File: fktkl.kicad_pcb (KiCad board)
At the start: 2 copper layers, 342.6 x 94.5 mm, 160 parts, among them K1 SCaps, K10 Z, K11 Super, K12 2, K13 W, K14 S, K15 X, K16 Alt, K17 3, K18 E, K19 D, K2 Esc, K20 C, K21 Space, K22 4, K23 R, K24 F, K25 V, K26 AltGr, K26 Space, K27 5, K28 T, K29 G, K3 Tab, K30 B, K31 Ctrl, K32 6, K33 Y, K34 H, K35 N, K36 Super, K37 7, K38 U, K39 J, K4 Caps, K40 M, K41 Left, K42 8, K43 I, K44 K, K45 ,, K46 Down, K47 9, K48 O, K49 L, K5 Shift, K50 ., K51 Right, K52 0, K53 P, K54 :, K55 -, K56 [, K57 ", K58 =, K59 ], K6 Ctrl, K60 /, K61 Yen, K62 |, K63 Shift, K64 BS, K65 Del, K66 Fn, K67 Ins, K68 Enter, K69 C3, K7 1, K70 Home, K71 C0, K72 Up, K73 PgUp, K74 C1, K75 C4, K76 End, K77 C2, K78 PgDwn, K8 Q, K9 A, U1 ProMicro

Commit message: connected row7
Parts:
- K26: value Space -> AltGr
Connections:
- U1 pad 14: Net-(U1-Pad14) -> /row7
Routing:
- net /row7: track 143.2 -> 237.0 mm
- net GND: track 95.5 -> 130.8 mm, vias 14 -> 16
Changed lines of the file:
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@@
 (kicad_pcb (version 4) (host pcbnew 4.0.7)
   (general
-    (links 548)
+    (links 549)
     (no_connects 0)
     (area 30.805779 28.7814 378.767951 126.494201)
     (thickness 1.6)
     (drawings 10)
-    (tracks 718)
+    (tracks 734)
     (zones 0)
     (modules 160)
-    (nets 101)
+    (nets 100)
   )
   (page A3)
@@
     (pad_to_mask_clearance 0.2)
     (aux_axis_origin 0 0)
-    (visible_elements 7FFFF77F)
+    (visible_elements 7FFFFFFF)
     (pcbplotparams
       (layerselection 0x010fc_80000001)
@@
   (net 96 /row7)
   (net 97 "Net-(U1-Pad1)")
-  (net 98 "Net-(U1-Pad14)")
-  (net 99 VCC)
-  (net 100 "Net-(Reset1-Pad2)")
+  (net 98 VCC)
+  (net 99 "Net-(Reset1-Pad2)")
   (net_class Default "This is the default net class."
     (clearance 0.2)
@@
     (add_net "Net-(Reset1-Pad2)")
     (add_net "Net-(U1-Pad1)")
-    (add_net "Net-(U1-Pad14)")
     (add_net VCC)
   )
@@
       (effects (font (size 1 1) (thickness 0.2)))
     )
-    (fp_text value Space (at 0 4.572) (layer F.SilkS)
+    (fp_text value AltGr (at 0 4.572) (layer F.SilkS)
       (effects (font (thickness 0.3048)))
     )
@@
       (net 93 GND))
     (pad 3 thru_hole circle (at -7.62 7.366 270) (size 1.7526 1.7526) (drill 1.0922) (layers *.Cu *.SilkS *.Mask)
-      (net 100 "Net-(Reset1-Pad2)"))
+      (net 99 "Net-(Reset1-Pad2)"))
     (pad 4 thru_hole circle (at -7.62 4.826 270) (size 1.7526 1.7526) (drill 1.0922) (layers *.Cu *.SilkS *.Mask)
-      (net 99 VCC))
+      (net 98 VCC))
     (pad 5 thru_hole circle (at -7.62 2.286 270) (size 1.7526 1.7526) (drill 1.0922) (layers *.Cu *.SilkS *.Mask)
       (net 90 /col7))
@@
       (net 93 GND))
     (pad 14 thru_hole circle (at 7.62 9.906 270) (size 1.7526 1.7526) (drill 1.0922) (layers *.Cu *.SilkS *.Mask)
-      (net 98 "Net-(U1-Pad14)"))
+      (net 96 /row7))
     (pad 13 thru_hole circle (at 7.62 12.446 270) (size 1.7526 1.7526) (drill 1.0922) (layers *.Cu *.SilkS *.Mask)
       (net 2 /row0))
@@
       (net 93 GND))
     (pad 2 smd rect (at -3.1 -1.85) (size 1.8 1.1) (layers B.Cu B.Paste B.Mask)
-      (net 100 "Net-(Reset1-Pad2)"))
+      (net 99 "Net-(Reset1-Pad2)"))
     (pad 2 smd rect (at 3.1 -1.85) (size 1.8 1.1) (layers B.Cu B.Paste B.Mask)
-      (net 100 "Net-(Reset1-Pad2)"))
+      (net 99 "Net-(Reset1-Pad2)"))
     (model ${KISYS3DMOD}/Buttons_Switches_SMD.3dshapes/SW_SPST_TL3342.wrl
       (at (xyz 0 0 0))
@@
   (segment (start 208.52625 46.73625) (end 218.05125 56.26125) (width 0.25) (layer F.Cu) (net 92))
   (segment (start 338.582 50.038) (end 339.09 50.038) (width 0.25) (layer B.Cu) (net 92) (status 30))
+  (segment (start 305.562 49.022) (end 285.75 49.022) (width 0.25) (layer B.Cu) (net 93))
+  (via (at 285.75 49.022) (size 0.6) (drill 0.4) (layers F.Cu B.Cu) (net 93))
+  (segment (start 318.516 55.118) (end 312.42 49.022) (width 0.25) (layer F.Cu) (net 93))
+  (segment (start 312.42 49.022) (end 305.562 49.022) (width 0.25) (layer F.Cu) (net 93))
+  (via (at 305.562 49.022) (size 0.6) (drill 0.4) (layers F.Cu B.Cu) (net 93))
   (segment (start 338.582 34.798) (end 340.868 34.798) (width 0.25) (layer F.Cu) (net 93) (status 10))
   (via (at 342.9 32.766) (size 0.6) (drill 0.4) (layers F.Cu B.Cu) (net 93))
@@
   (segment (start 269.08125 63.43125) (end 288.13125 63.43125) (width 0.25) (layer B.Cu) (net 95))
   (segment (start 250.03125 63.43125) (end 269.08125 63.43125) (width 0.25) (layer B.Cu) (net 95))
+  (segment (start 273.84375 82.48125) (end 273.84375 81.43125) (width 0.25) (layer F.Cu) (net 96))
+  (segment (start 273.84375 81.43125) (end 276.287349 78.987651) (width 0.25) (layer F.Cu) (net 96))
+  (segment (start 276.287349 78.987651) (end 276.287349 57.976651) (width 0.25) (layer F.Cu) (net 96))
+  (segment (start 321.564 33.02) (end 322.465701 33.921701) (width 0.25) (layer F.Cu) (net 96))
+  (segment (start 276.287349 57.976651) (end 279.4 54.864) (width 0.25) (layer F.Cu) (net 96))
+  (segment (start 279.4 54.864) (end 279.4 47.752) (width 0.25) (layer F.Cu) (net 96))
+  (segment (start 279.4 47.752) (end 280.924 46.228) (width 0.25) (layer F.Cu) (net 96))
+  (segment (start 280.924 46.228) (end 280.924 36.068) (width 0.25) (layer F.Cu) (net 96))
+  (segment (start 280.924 36.068) (end 283.972 33.02) (width 0.25) (layer F.Cu) (net 96))
+  (segment (start 283.972 33.02) (end 321.564 33.02) (width 0.25) (layer F.Cu) (net 96))
+  (segment (start 322.465701 33.921701) (end 323.342 34.798) (width 0.25) (layer F.Cu) (net 96))
   (segment (start 358.14 101.436) (end 361.188 101.436) (width 0.25) (layer B.Cu) (net 96))
   (segment (start 340.51875 101.53125) (end 358.04475 101.53125) (width 0.25) (layer B.Cu) (net 96))
@@
   (segment (start 273.84375 99.28225) (end 271.59475 101.53125) (width 0.25) (layer F.Cu) (net 96))
   (segment (start 254.79375 82.48125) (end 273.84375 82.48125) (width 0.25) (layer B.Cu) (net 96))
-  (segment (start 353.262 48.188) (end 359.462 48.188) (width 0.25) (layer B.Cu) (net 100))
-  (segment (start 353.262 48.188) (end 345.622 48.188) (width 0.25) (layer B.Cu) (net 100))
-  (segment (start 339.852 37.846) (end 339.344 37.338) (width 0.25) (layer F.Cu) (net 100) (status 20))
-  (segment (start 339.852 40.132) (end 339.852 37.846) (width 0.25) (layer F.Cu) (net 100))
-  (segment (start 340.36 40.64) (end 339.852 40.132) (width 0.25) (layer F.Cu) (net 100))
-  (segment (start 342.392 40.64) (end 340.36 40.64) (width 0.25) (layer F.Cu) (net 100))
-  (segment (start 343.154 41.402) (end 342.392 40.64) (width 0.25) (layer F.Cu) (net 100))
-  (segment (start 343.154 45.72) (end 343.154 41.402) (width 0.25) (layer F.Cu) (net 100))
-  (via (at 343.154 45.72) (size 0.6) (drill 0.4) (layers F.Cu B.Cu) (net 100))
-  (segment (start 345.622 48.188) (end 343.154 45.72) (width 0.25) (layer B.Cu) (net 100))
-  (segment (start 339.344 37.338) (end 338.582 37.338) (width 0.25) (layer F.Cu) (net 100) (status 30))
-  (segment (start 338.074 37.846) (end 338.582 37.338) (width 0.25) (layer F.Cu) (net 100) (status 30))
+  (segment (start 353.262 48.188) (end 359.462 48.188) (width 0.25) (layer B.Cu) (net 99))
+  (segment (start 353.262 48.188) (end 345.622 48.188) (width 0.25) (layer B.Cu) (net 99))
+  (segment (start 339.852 37.846) (end 339.344 37.338) (width 0.25) (layer F.Cu) (net 99) (status 20))
+  (segment (start 339.852 40.132) (end 339.852 37.846) (width 0.25) (layer F.Cu) (net 99))
+  (segment (start 340.36 40.64) (end 339.852 40.132) (width 0.25) (layer F.Cu) (net 99))
+  (segment (start 342.392 40.64) (end 340.36 40.64) (width 0.25) (layer F.Cu) (net 99))
+  (segment (start 343.154 41.402) (end 342.392 40.64) (width 0.25) (layer F.Cu) (net 99))
+  (segment (start 343.154 45.72) (end 343.154 41.402) (width 0.25) (layer F.Cu) (net 99))
+  (via (at 343.154 45.72) (size 0.6) (drill 0.4) (layers F.Cu B.Cu) (net 99))
+  (segment (start 345.622 48.188) (end 343.154 45.72) (width 0.25) (layer B.Cu) (net 99))
+  (segment (start 339.344 37.338) (end 338.582 37.338) (width 0.25) (layer F.Cu) (net 99) (status 30))
+  (segment (start 338.074 37.846) (end 338.582 37.338) (width 0.25) (layer F.Cu) (net 99) (status 30))
   (zone (net 93) (net_name GND) (layer F.Cu) (hatch edge 0.508)
     (connect_pads (clearance 0.508))

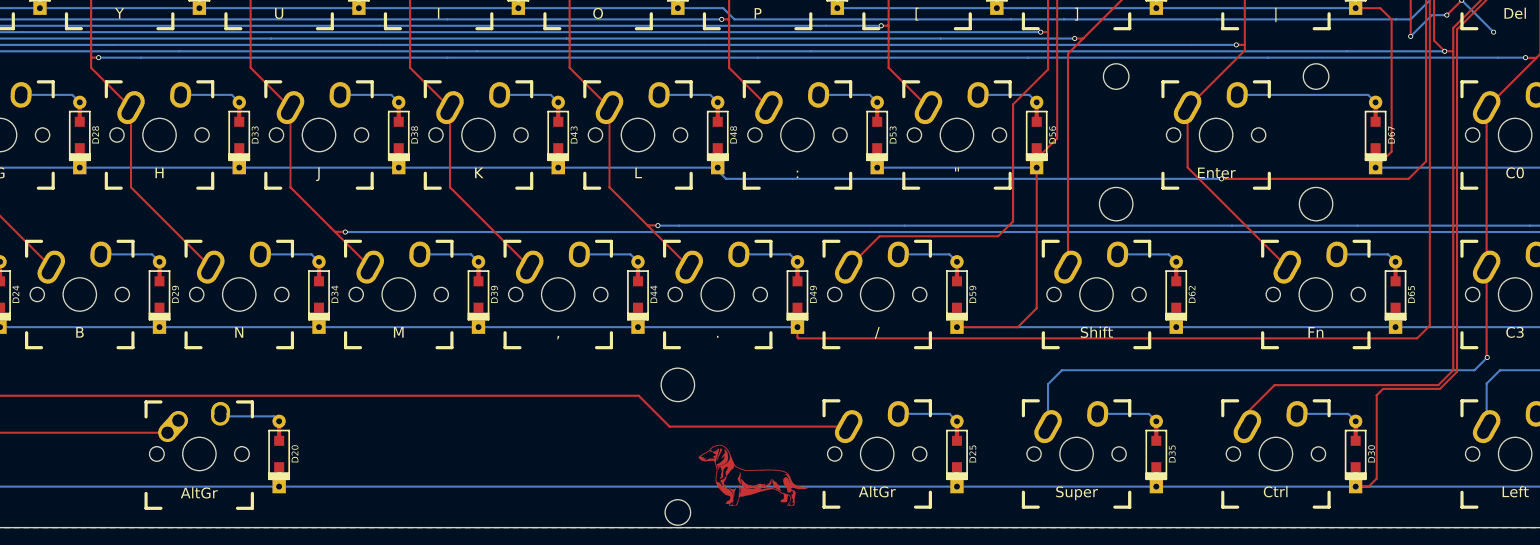
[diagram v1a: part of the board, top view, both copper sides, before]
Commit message: switche left ctrl and left gui
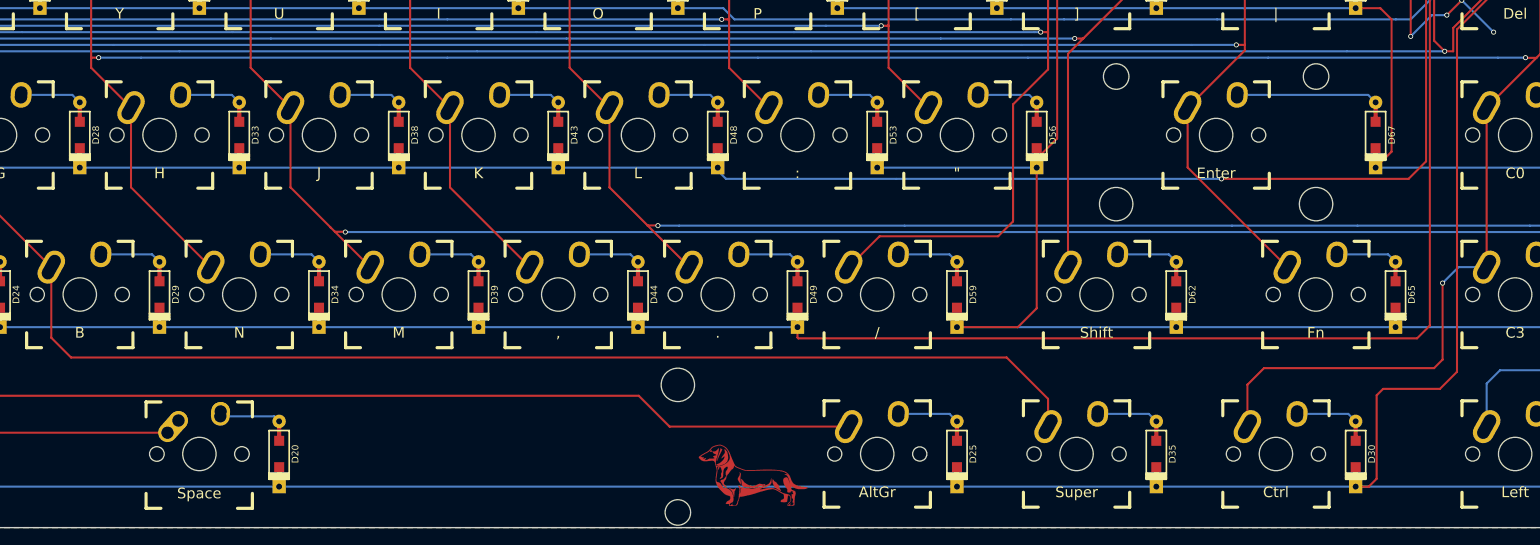
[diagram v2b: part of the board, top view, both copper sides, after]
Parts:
- K26: value AltGr -> Space
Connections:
- K31 pad 1: /col5 -> /col6
- K36 pad 1: /col6 -> /col5
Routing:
- net /col5: track 379.1 -> 446.4 mm
- net /col6: track 384.9 -> 358.4 mm
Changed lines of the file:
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@@
     (links 549)
     (no_connects 0)
-    (area 30.805779 28.7814 378.767951 126.494201)
+    (area 33.452999 30.912999 376.249001 125.551001)
     (thickness 1.6)
     (drawings 10)
-    (tracks 734)
+    (tracks 733)
     (zones 0)
     (modules 160)
@@
     (pad_to_mask_clearance 0.2)
     (aux_axis_origin 0 0)
+    (grid_origin 38.354 -9.398)
     (visible_elements 7FFFFFFF)
     (pcbplotparams
@@
       (effects (font (size 1 1) (thickness 0.2)))
     )
-    (fp_text value AltGr (at 0 4.572) (layer F.SilkS)
+    (fp_text value Space (at 0 4.572) (layer F.SilkS)
       (effects (font (thickness 0.3048)))
     )
@@
     (pad HOLE np_thru_hole circle (at 5.08 0) (size 1.7018 1.7018) (drill 1.7018) (layers *.Cu))
     (pad 1 thru_hole oval (at -3.405 -3.27 330.95) (size 2.5 4.17) (drill oval 1.5 3.17) (layers *.Cu *.Mask F.SilkS)
-      (net 88 /col5))
+      (net 89 /col6))
     (pad 2 thru_hole oval (at 2.52 -4.79 356.1) (size 2.5 3.08) (drill oval 1.5 2.08) (layers *.Cu *.Mask F.SilkS)
       (net 35 "Net-(D30-Pad2)"))
@@
     (pad HOLE np_thru_hole circle (at 5.08 0) (size 1.7018 1.7018) (drill 1.7018) (layers *.Cu))
     (pad 1 thru_hole oval (at -3.405 -3.27 330.95) (size 2.5 4.17) (drill oval 1.5 3.17) (layers *.Cu *.Mask F.SilkS)
-      (net 89 /col6))
+      (net 88 /col5))
     (pad 2 thru_hole oval (at 2.52 -4.79 356.1) (size 2.5 3.08) (drill oval 1.5 2.08) (layers *.Cu *.Mask F.SilkS)
       (net 40 "Net-(D35-Pad2)"))
@@
   (segment (start 113.27625 37.21125) (end 113.27625 46.73625) (width 0.25) (layer F.Cu) (net 87))
   (segment (start 113.27625 46.73625) (end 122.80125 56.26125) (width 0.25) (layer F.Cu) (net 87))
+  (segment (start 275.20125 113.41125) (end 275.20125 110.10125) (width 0.25) (layer F.Cu) (net 88))
+  (segment (start 156.13875 102.79875) (end 156.13875 94.36125) (width 0.25) (layer F.Cu) (net 88))
+  (segment (start 158.496 105.156) (end 156.13875 102.79875) (width 0.25) (layer F.Cu) (net 88))
+  (segment (start 270.256 105.156) (end 158.496 105.156) (width 0.25) (layer F.Cu) (net 88))
+  (segment (start 275.20125 110.10125) (end 270.256 105.156) (width 0.25) (layer F.Cu) (net 88))
   (segment (start 338.582 55.118) (end 336.804 55.118) (width 0.25) (layer B.Cu) (net 88) (status 10))
   (segment (start 331.272 52.578) (end 327.58875 56.26125) (width 0.25) (layer B.Cu) (net 88))
@@
   (segment (start 142.748 68.58) (end 145.034 68.58) (width 0.25) (layer B.Cu) (net 88))
   (via (at 142.748 68.58) (size 0.6) (drill 0.4) (layers F.Cu B.Cu) (net 88))
-  (segment (start 299.01375 113.41125) (end 299.01375 111.70425) (width 0.25) (layer F.Cu) (net 88))
-  (segment (start 299.01375 111.70425) (end 302.26 108.458) (width 0.25) (layer F.Cu) (net 88))
-  (segment (start 323.596 89.408) (end 323.596 68.58) (width 0.25) (layer F.Cu) (net 88))
-  (segment (start 323.596 106.68) (end 323.596 89.408) (width 0.25) (layer F.Cu) (net 88))
-  (segment (start 321.818 108.458) (end 323.596 106.68) (width 0.25) (layer F.Cu) (net 88))
-  (segment (start 302.26 108.458) (end 321.818 108.458) (width 0.25) (layer F.Cu) (net 88))
   (segment (start 323.596 68.58) (end 323.596 65.786) (width 0.25) (layer F.Cu) (net 88))
   (segment (start 327.58875 61.79325) (end 327.58875 56.26125) (width 0.25) (layer F.Cu) (net 88))
@@
   (segment (start 132.32625 37.21125) (end 132.32625 46.73625) (width 0.25) (layer F.Cu) (net 88))
   (segment (start 132.32625 46.73625) (end 141.85125 56.26125) (width 0.25) (layer F.Cu) (net 88))
-  (segment (start 275.20125 113.41125) (end 275.20125 108.33875) (width 0.25) (layer B.Cu) (net 89))
-  (segment (start 327.58875 105.08475) (end 327.58875 94.36125) (width 0.25) (layer F.Cu) (net 89))
-  (segment (start 327.66 105.156) (end 327.58875 105.08475) (width 0.25) (layer F.Cu) (net 89))
-  (via (at 327.66 105.156) (size 0.6) (drill 0.4) (layers F.Cu B.Cu) (net 89))
-  (segment (start 326.136 106.68) (end 327.66 105.156) (width 0.25) (layer B.Cu) (net 89))
-  (segment (start 276.86 106.68) (end 326.136 106.68) (width 0.25) (layer B.Cu) (net 89))
-  (segment (start 275.20125 108.33875) (end 276.86 106.68) (width 0.25) (layer B.Cu) (net 89))
-  (segment (start 275.20125 113.41125) (end 275.20125 111.64075) (width 0.25) (layer B.Cu) (net 89))
+  (segment (start 299.01375 113.41125) (end 299.01375 108.40225) (width 0.25) (layer F.Cu) (net 89))
+  (segment (start 324.23075 94.36125) (end 327.58875 94.36125) (width 0.25) (layer B.Cu) (net 89))
+  (segment (start 322.326 96.266) (end 324.23075 94.36125) (width 0.25) (layer B.Cu) (net 89))
+  (via (at 322.326 96.266) (size 0.6) (drill 0.4) (layers F.Cu B.Cu) (net 89))
+  (segment (start 322.326 105.41) (end 322.326 96.266) (width 0.25) (layer F.Cu) (net 89))
+  (segment (start 321.31 106.426) (end 322.326 105.41) (width 0.25) (layer F.Cu) (net 89))
+  (segment (start 300.99 106.426) (end 321.31 106.426) (width 0.25) (layer F.Cu) (net 89))
+  (segment (start 299.01375 108.40225) (end 300.99 106.426) (width 0.25) (layer F.Cu) (net 89))
+  (segment (start 299.01375 113.41125) (end 299.01375 111.70425) (width 0.25) (layer F.Cu) (net 89))
   (segment (start 338.582 57.658) (end 334.518 57.658) (width 0.25) (layer F.Cu) (net 89) (status 10))
   (segment (start 160.90125 69.342) (end 161.798 69.342) (width 0.25) (layer F.Cu) (net 89))
@@
   (via (at 161.798 69.342) (size 0.6) (drill 0.4) (layers F.Cu B.Cu) (net 89))
   (segment (start 327.58875 94.36125) (end 327.58875 92.63875) (width 0.25) (layer B.Cu) (net 89))
-  (segment (start 275.20125 113.41125) (end 275.20125 111.89475) (width 0.25) (layer F.Cu) (net 89))
   (segment (start 334.01 68.89) (end 333.53 69.37) (width 0.25) (layer F.Cu) (net 89))
   (segment (start 333.53 69.37) (end 327.58875 75.31125) (width 0.25) (layer F.Cu) (net 89))
